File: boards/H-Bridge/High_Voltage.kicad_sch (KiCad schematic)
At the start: 26 parts, among them IC2 MIC4606-1YML-TR, IC3 AD8410AWBRZ-RL, J1 V+, J2 V-, J3 Motor-, J4 Motor+, J9 12V+, M1 Motor_DC, Q1 NTBLS4D0N15MC, Q2 NTBLS4D0N15MC, Q3 NTBLS4D0N15MC, Q4 NTBLS4D0N15MC

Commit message: FET layout nearing completion
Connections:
- net SHUNT+: now also Q1.1 (S_1), Q1.2 (S_2), Q1.3 (S_3), Q1.4 (S_4), Q1.5 (S_5), Q1.6 (S_6), Q1.7 (S_7), Q2.10 (D_2), Q2.11 (D_3), Q2.12 (D_4), Q2.13 (D_5), Q2.9 (D_1), R1.1, R12.1; no longer J4.1 (Pin_1), M1.1 (+), R1.2
- net SHUNT-: now also J4.1 (Pin_1), M1.1 (+), R1.2; no longer Q1.1 (S_1), Q1.2 (S_2), Q1.3 (S_3), Q1.4 (S_4), Q1.5 (S_5), Q1.6 (S_6), Q1.7 (S_7), Q2.10 (D_2), Q2.11 (D_3), Q2.12 (D_4), Q2.13 (D_5), Q2.9 (D_1), R1.1, R12.1
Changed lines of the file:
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@@
+	)
+	(junction
+		(at 186.69 69.85)
+		(diameter 0)
+		(color 0 0 0 0)
 	)
 	(junction
@@
 		(color 0 0 0 0)
 	)
-	(junction
-		(at 186.69 69.85)
-		(diameter 0)
-		(color 0 0 0 0)
-	)
 	(no_connect
 		(at 55.88 82.55)
@@
 	(wire
 		(pts
+			(xy 195.58 72.39) (xy 195.58 69.85)
+		)
+		(stroke
+			(width 0)
+			(type default)
+		)
+	)
+	(wire
+		(pts
 			(xy 144.78 88.9) (xy 143.51 88.9)
 		)
@@
 	(wire
 		(pts
+			(xy 186.69 72.39) (xy 186.69 69.85)
+		)
+		(stroke
+			(width 0)
+			(type default)
+		)
+	)
+	(wire
+		(pts
 			(xy 243.84 46.99) (xy 246.38 46.99)
 		)
@@
 	(wire
 		(pts
-			(xy 195.58 73.66) (xy 195.58 69.85)
-		)
-		(stroke
-			(width 0)
-			(type default)
-		)
-	)
-	(wire
-		(pts
 			(xy 54.61 50.8) (xy 55.88 50.8)
 		)
@@
 		(pts
 			(xy 58.42 43.18) (xy 58.42 52.07)
-		)
-		(stroke
-			(width 0)
-			(type default)
-		)
-	)
-	(wire
-		(pts
-			(xy 186.69 73.66) (xy 186.69 69.85)
 		)
 		(stroke
@@
 	)
 	(label "SHUNT+"
-		(at 195.58 73.66 270)
+		(at 186.69 72.39 270)
 		(effects
 			(font
@@
 	)
 	(label "SHUNT-"
-		(at 186.69 73.66 270)
+		(at 195.58 72.39 270)
 		(effects
 			(font

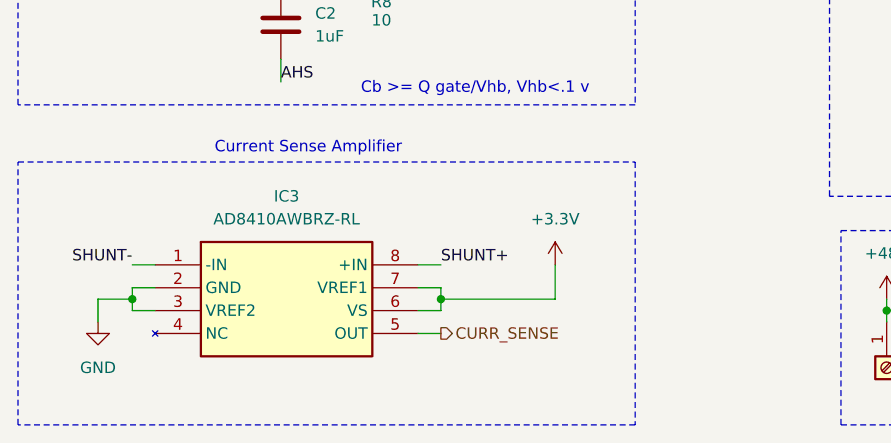
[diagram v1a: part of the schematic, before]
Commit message: finished layout, need to add silk key
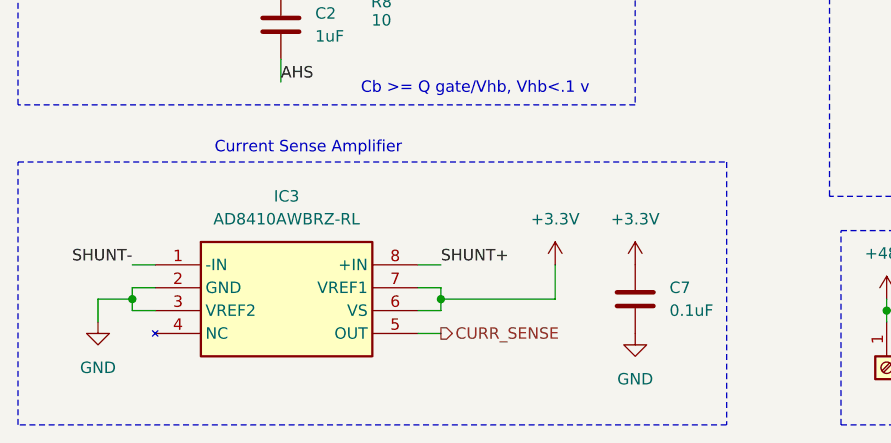
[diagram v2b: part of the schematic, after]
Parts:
- added C7: 0.1uF, symbol Device:C
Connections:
- net +3.3V: now also C7.1
- net GND: now also C7.2
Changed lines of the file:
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@@
 	(rectangle
 		(start 29.21 109.22)
-		(end 97.79 138.43)
+		(end 107.95 138.43)
 		(stroke
 			(width 0)
@@
 	)
 	(symbol
+		(lib_id "Device:C")
+		(at 97.79 124.46 0)
+		(unit 1)
+		(body_style 1)
+		(exclude_from_sim no)
+		(in_bom yes)
+		(on_board yes)
+		(in_pos_files yes)
+		(dnp no)
+		(fields_autoplaced yes)
+		(property "Reference" "C7"
+			(at 101.6 123.1899 0)
+			(show_name no)
+			(do_not_autoplace no)
+			(effects
+				(font
+					(size 1.27 1.27)
+				)
+				(justify left)
+			)
+		)
+		(property "Value" "0.1uF"
+			(at 101.6 125.7299 0)
+			(show_name no)
+			(do_not_autoplace no)
+			(effects
+				(font
+					(size 1.27 1.27)
+				)
+				(justify left)
+			)
+		)
+		(property "Footprint" ""
+			(at 98.7552 128.27 0)
+			(hide yes)
+			(show_name no)
+			(do_not_autoplace no)
+			(effects
+				(font
+					(size 1.27 1.27)
+				)
+			)
+		)
+		(property "Datasheet" ""
+			(at 97.79 124.46 0)
+			(hide yes)
+			(show_name no)
+			(do_not_autoplace no)
+			(effects
+				(font
+					(size 1.27 1.27)
+				)
+			)
+		)
+		(property "Description" "Unpolarized capacitor"
+			(at 97.79 124.46 0)
+			(hide yes)
+			(show_name no)
+			(do_not_autoplace no)
+			(effects
+				(font
+					(size 1.27 1.27)
+				)
+			)
+		)
+		(pin "2"
+		)
+		(pin "1"
+		)
+		(instances
+			(project "brushed_v2"
+				(path "/eb8a71f1-dfd1-4787-8d20-e1c5cbb51f86/576e7c9a-0307-4216-9e33-6884784be1ad"
+					(reference "C7")
+					(unit 1)
+				)
+			)
+		)
+	)
+	(symbol
 		(lib_id "power:GND")
 		(at 142.24 130.81 0)
@@
 	)
 	(symbol
+		(lib_id "power:GND")
+		(at 97.79 128.27 0)
+		(unit 1)
+		(body_style 1)
+		(exclude_from_sim no)
+		(in_bom yes)
+		(on_board yes)
+		(in_pos_files yes)
+		(dnp no)
+		(fields_autoplaced yes)
+		(property "Reference" "#PWR060"
+			(at 97.79 134.62 0)
+			(hide yes)
+			(show_name no)
+			(do_not_autoplace no)
+			(effects
+				(font
+					(size 1.27 1.27)
+				)
+			)
+		)
+		(property "Value" "GND"
+			(at 97.79 133.35 0)
+			(show_name no)
+			(do_not_autoplace no)
+			(effects
+				(font
+					(size 1.27 1.27)
+				)
+			)
+		)
+		(property "Footprint" ""
+			(at 97.79 128.27 0)
+			(hide yes)
+			(show_name no)
+			(do_not_autoplace no)
+			(effects
+				(font
+					(size 1.27 1.27)
+				)
+			)
+		)
+		(property "Datasheet" ""
+			(at 97.79 128.27 0)
+			(hide yes)
+			(show_name no)
+			(do_not_autoplace no)
+			(effects
+				(font
+					(size 1.27 1.27)
+				)
+			)
+		)
+		(property "Description" "Power symbol creates a global label with name \"GND\" , ground"
+			(at 97.79 128.27 0)
+			(hide yes)
+			(show_name no)
+			(do_not_autoplace no)
+			(effects
+				(font
+					(size 1.27 1.27)
+				)
+			)
+		)
+		(pin "1"
+		)
+		(instances
+			(project "brushed_v2"
+				(path "/eb8a71f1-dfd1-4787-8d20-e1c5cbb51f86/576e7c9a-0307-4216-9e33-6884784be1ad"
+					(reference "#PWR060")
+					(unit 1)
+				)
+			)
+		)
+	)
+	(symbol
 		(lib_id "Device:R_US")
 		(at 215.9 67.31 270)
@@
 					(unit 1)
 				)
+			)
+		)
+	)
+	(symbol
+		(lib_id "power:+3.3V")
+		(at 97.79 120.65 0)
+		(unit 1)
+		(body_style 1)
+		(exclude_from_sim no)
+		(in_bom yes)
+		(on_board yes)
+		(in_pos_files yes)
+		(dnp no)
+		(fields_autoplaced yes)
+		(property "Reference" "#PWR059"
+			(at 97.79 124.46 0)
+			(hide yes)
+			(show_name no)
+			(do_not_autoplace no)
+			(effects
+				(font
+					(size 1.27 1.27)
+				)
+			)
+		)
+		(property "Value" "+3.3V"
+			(at 97.79 115.57 0)
+			(show_name no)
+			(do_not_autoplace no)
+			(effects
+				(font
+					(size 1.27 1.27)
+				)
+			)
+		)
+		(property "Footprint" ""
+			(at 97.79 120.65 0)
+			(hide yes)
+			(show_name no)
+			(do_not_autoplace no)
+			(effects
+				(font
+					(size 1.27 1.27)
+				)
+			)
+		)
+		(property "Datasheet" ""
+			(at 97.79 120.65 0)
+			(hide yes)
+			(show_name no)
+			(do_not_autoplace no)
+			(effects
+				(font
+					(size 1.27 1.27)
+				)
+			)
+		)
+		(property "Description" "Power symbol creates a global label with name \"+3.3V\""
+			(at 97.79 120.65 0)
+			(hide yes)
+			(show_name no)
+			(do_not_autoplace no)
+			(effects
+				(font
+					(size 1.27 1.27)
+				)
+			)
+		)
+		(pin "1"
+		)
+		(instances
+			(project "brushed_v2"
+				(path "/eb8a71f1-dfd1-4787-8d20-e1c5cbb51f86/576e7c9a-0307-4216-9e33-6884784be1ad"
+					(reference "#PWR059")
+					(unit 1)
+				)
